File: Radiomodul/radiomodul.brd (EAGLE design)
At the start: 74 x 59 mm, 39 parts, among them IC1 ATMEGA2561-16AI, IC2 MCP42050, IC3 E910.15, IC4 AVR-JTAG, IC5 MAX232ECWE, IC6 MCP601SN, IC7 TLE42754D, J1 39-30-1100, Q1 14,7456

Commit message: some parts changed, BOM added
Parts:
- D3: value (none) -> S1J
- Q1: value 14,7456 -> 16000000
- R6: value 5k -> 4k7
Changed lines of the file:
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@@
 <attribute name="NAME" x="53.975" y="38.735" size="1.27" layer="25" rot="R45"/>
 </element>
-<element name="Q1" library="crystal" library_urn="urn:adsk.eagle:library:204" package="HC49UP" package3d_urn="urn:adsk.eagle:package:12078/1" value="14,7456" x="34.925" y="7.62" smashed="yes" rot="R180">
+<element name="Q1" library="crystal" library_urn="urn:adsk.eagle:library:204" package="HC49UP" package3d_urn="urn:adsk.eagle:package:12078/1" value="16000000" x="34.925" y="7.62" smashed="yes" rot="R180">
 <attribute name="MF" value="" x="34.925" y="7.62" size="1.778" layer="27" rot="R180" display="off"/>
 <attribute name="MPN" value="" x="34.925" y="7.62" size="1.778" layer="27" rot="R180" display="off"/>
@@
 <attribute name="SPICEPREFIX" value="R" x="24.13" y="37.465" size="1.778" layer="27" rot="R180" display="off"/>
 </element>
-<element name="R6" library="rcl" library_urn="urn:adsk.eagle:library:334" package="R0805" package3d_urn="urn:adsk.eagle:package:23553/2" value="5k" x="19.05" y="51.435" smashed="yes" rot="R90">
+<element name="R6" library="rcl" library_urn="urn:adsk.eagle:library:334" package="R0805" package3d_urn="urn:adsk.eagle:package:23553/2" value="4k7" x="19.05" y="51.435" smashed="yes" rot="R90">
 <attribute name="NAME" x="19.685" y="53.975" size="1.27" layer="25" rot="R90"/>
 <attribute name="SPICEPREFIX" value="R" x="19.05" y="51.435" size="1.778" layer="27" rot="R90" display="off"/>
@@
 <attribute name="SPICEPREFIX" value="C" x="35.56" y="32.385" size="1.778" layer="27" display="off"/>
 </element>
-<element name="D3" library="Heinrich" package="SMADIODE" value="" x="8.89" y="36.83" smashed="yes" rot="R180">
+<element name="D3" library="Heinrich" package="SMADIODE" value="S1J" x="8.89" y="36.83" smashed="yes" rot="R180">
 <attribute name="NAME" x="3.175" y="38.1" size="1.27" layer="25" rot="R270"/>
 <attribute name="VALUE" x="11.43" y="39.116" size="0.4064" layer="27" font="vector" rot="R180"/>

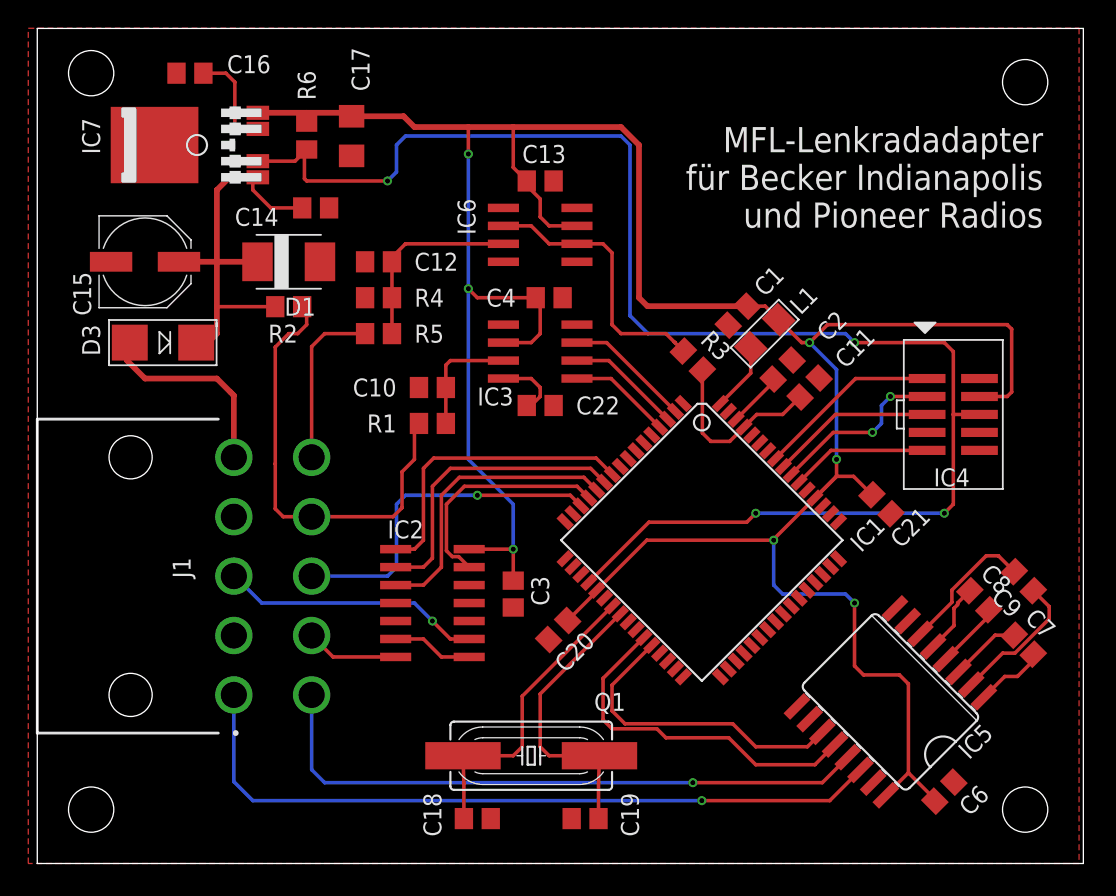
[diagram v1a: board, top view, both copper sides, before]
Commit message: board and schematic replaced
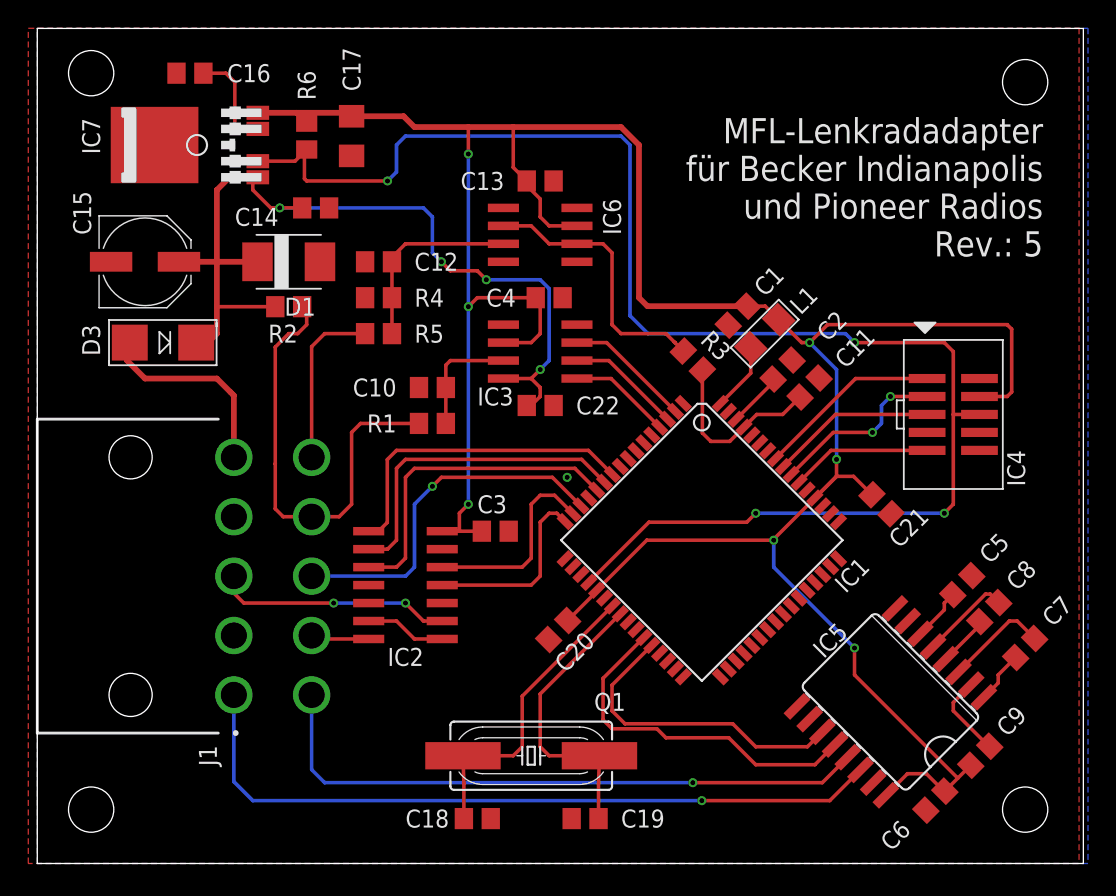
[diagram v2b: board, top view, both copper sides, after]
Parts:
- added C5: 1uF, rcl:C0805
- C18, C19: value 18pF -> 22pF
- C6, C7, C8, C9: value 100nF -> 1uF
- moved C9 12.7 mm to (66.7, 7.62), turned to 225 degrees
- moved C3 4.62 mm to (32.4, 23.5), turned to 0 degrees
- moved IC2 2.29 mm to (26.0, 19.7)
- moved C8 1.09 mm to (67.3, 17.8), turned to 225 degrees
- moved C6 0.90 mm to (63.5, 4.45), turned to 225 degrees
- moved C7 0.25 mm to (69.8, 15.2), turned to 225 degrees
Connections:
- net /CS renamed !CS
- net /RESET renamed !RESET
- removed net MISO: IC1.13, IC2.13
- removed net N$9 (its old number): C9.2, IC5.6
- removed net VBAT: C22.1, IC3.4
- new net !RS: IC1.16, IC2.11
- new net !SHDN: IC1.15, IC2.12
- new net N$3: C5.2, IC5.6
- net 5.0V: now also C9.2
- net GND: now also C5.1
- net SAFT: now also C22.1, IC3.4
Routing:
- net SAFT: track 29.9 -> 64.4 mm, vias 0 -> 4
- net MISO: track 16.3 -> 0.00 mm
- net !SHDN: track 0.00 -> 14.1 mm
- net !RS: track 0.00 -> 13.3 mm
- net N$9 (its old number): track 9.89 -> 0.00 mm
- net VBAT: track 4.71 -> 0.00 mm
- net 5.0V: track 200.4 -> 195.9 mm
- net N$10: track 9.90 -> 5.99 mm
- net N$3: track 0.00 -> 3.72 mm
- net PIONEER_1: track 6.57 -> 4.14 mm
- net N$4: track 5.02 -> 7.38 mm
- net MOSI: track 20.7 -> 23.0 mm
- net SCK: track 21.0 -> 23.0 mm
- net PIONEER_3: track 18.5 -> 16.8 mm, vias 1 -> 2
- net !CS: track 21.4 -> 22.9 mm
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- added copper zone on layer 16, net GND
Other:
- board text added: "MFL-Lenkradadapter für Becker Indianapolis und Pioneer Radios Rev.: 5"
- board text removed: "MFL-Lenkradadapter für Becker Indianapolis und Pioneer Radios"
